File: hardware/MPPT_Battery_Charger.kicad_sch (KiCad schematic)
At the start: 74 parts, among them Q24 SI7414DN-T1-E3, Q25 SI7414DN-T1-E3, Q5 SI7414DN-T1-E3, Q6 SI7414DN-T1-E3, Q8 SI2302DDS-T1-GE3, U22 BQ24650RVAT, U26 LMV321RIYLT, U28 LMV321RIYLT, U4 INA199C1DCKR

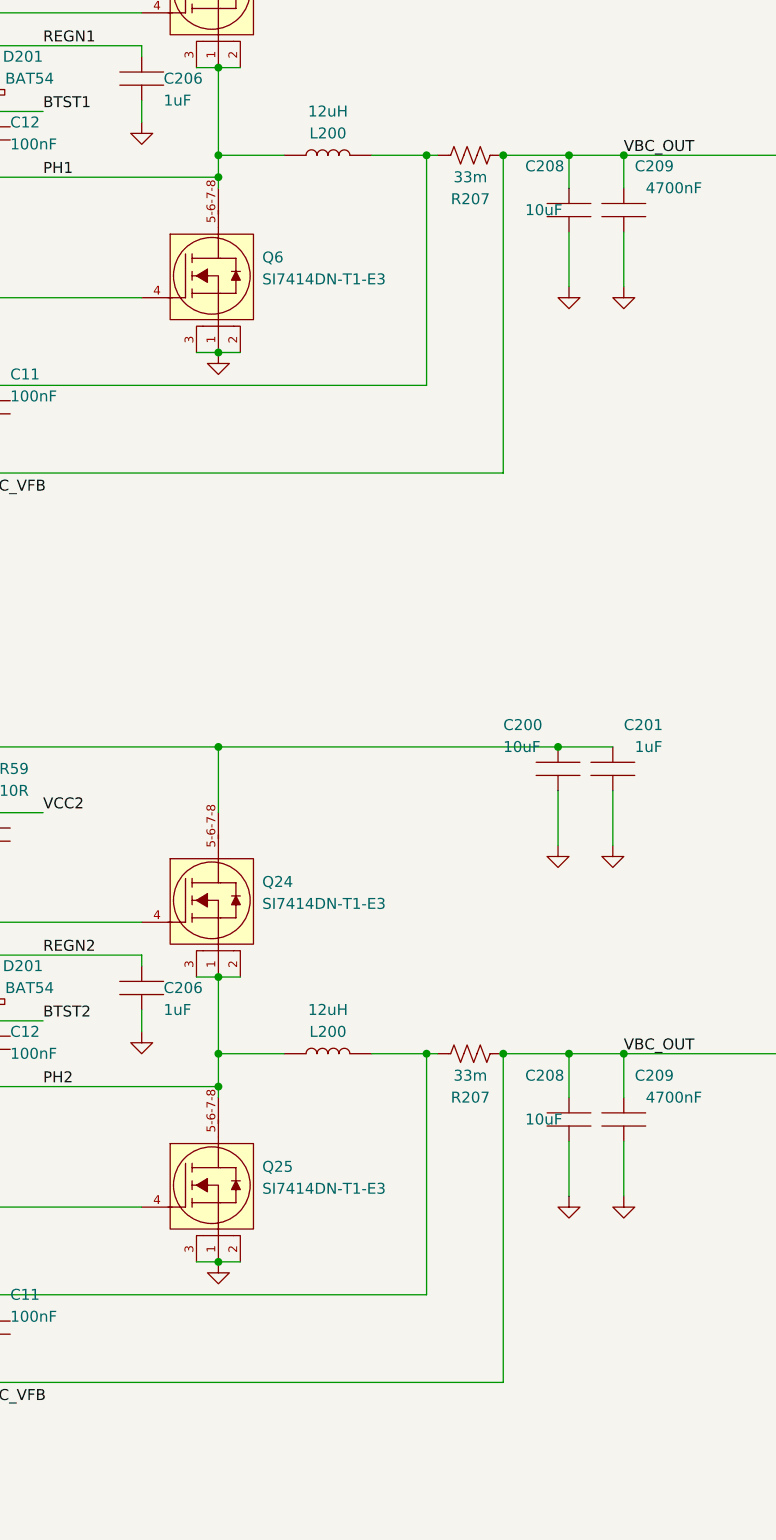
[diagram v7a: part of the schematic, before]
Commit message: hardware: Updating the schematic and layout to solve #8, #9 and #10.
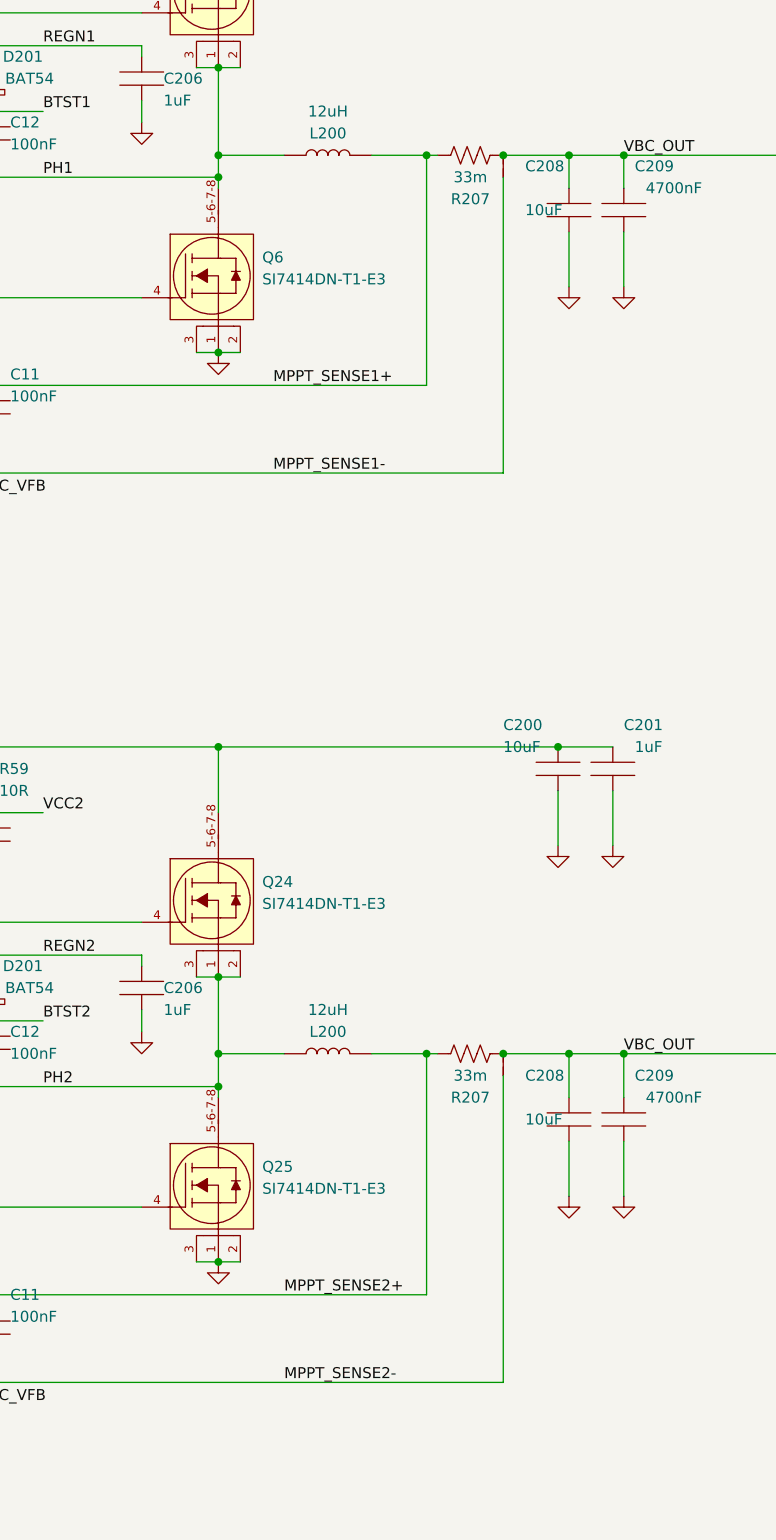
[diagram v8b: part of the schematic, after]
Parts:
- added JP2 (x2): SolderJumper_2_Bridged, footprints:Jumper, symbol Jumper:Jumper
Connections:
- net VBC_OUT: now also JP2.2 (B), JP2.2 (B); no longer C11.2, C11.2, U22.9 (SRN), U22.9 (SRN)
- net MPPT_SENSE1+: now reaches C11.1, L200.2, R207.2, U22.10 (SRP)
- net MPPT_SENSE2+: now reaches C11.1, L200.2, R207.2, U22.10 (SRP)
- new net MPPT_SENSE1-: C11.2, JP2.1 (A), U22.9 (SRN)
- new net MPPT_SENSE2-: C11.2, JP2.1 (A), U22.9 (SRN)
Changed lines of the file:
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@@
     (stroke (width 0) (type default))
   )
-  (wire (pts (xy 256.54 203.2) (xy 256.54 165.1))
+  (wire (pts (xy 256.54 203.2) (xy 256.54 167.64))
     (stroke (width 0) (type default))
   )
@@
     (stroke (width 0) (type default))
   )
-  (wire (pts (xy 256.54 97.79) (xy 256.54 60.96))
+  (wire (pts (xy 256.54 97.79) (xy 256.54 63.5))
     (stroke (width 0) (type default))
   )
@@
     (effects (font (size 1.27 1.27)) (justify left bottom))
   )
+  (label "MPPT_SENSE1-" (at 229.87 97.79 0) (fields_autoplaced)
+    (effects (font (size 1.27 1.27)) (justify left bottom))
+  )
   (label "AMUX3" (at 250.19 264.16 0) (fields_autoplaced)
     (effects (font (size 1.27 1.27)) (justify left bottom))
@@
     (effects (font (size 1.27 1.27)) (justify left bottom))
   )
+  (label "MPPT_SENSE1+" (at 229.87 87.63 0) (fields_autoplaced)
+    (effects (font (size 1.27 1.27)) (justify left bottom))
+  )
   (label "VBC_IN" (at 120.65 85.09 180) (fields_autoplaced)
     (effects (font (size 1.27 1.27)) (justify right bottom))
   )
+  (label "MPPT_SENSE2+" (at 231.14 193.04 0) (fields_autoplaced)
+    (effects (font (size 1.27 1.27)) (justify left bottom))
+  )
   (label "BC_VFB" (at 196.85 205.74 0) (fields_autoplaced)
     (effects (font (size 1.27 1.27)) (justify left bottom))
@@
     (effects (font (size 1.27 1.27)) (justify left bottom))
   )
+  (label "MPPT_SENSE2-" (at 231.14 203.2 0) (fields_autoplaced)
+    (effects (font (size 1.27 1.27)) (justify left bottom))
+  )
   (label "REGN1" (at 203.2 48.26 0) (fields_autoplaced)
     (effects (font (size 1.27 1.27)) (justify left bottom))
@@
     )
   )
+  (symbol (lib_id "Jumper:Jumper") (at 256.54 62.23 90) (unit 1)
+    (in_bom yes) (on_board yes) (dnp no) (fields_autoplaced)
+    (property "Reference" "JP2" (at 254.508 62.23 0)
+      (effects (font (size 1.27 1.27)) hide)
+    )
+    (property "Value" "SolderJumper_2_Bridged" (at 259.08 62.23 0)
+      (effects (font (size 1.27 1.27)) hide)
+    )
+    (property "Footprint" "footprints:Jumper" (at 256.54 62.23 0)
+      (effects (font (size 1.27 1.27)) hide)
+    )
+    (property "Datasheet" "~" (at 256.54 62.23 0)
+      (effects (font (size 1.27 1.27)) hide)
+    )
+    (pin "1")
+    (pin "2")
+    (instances
+      (project "eps-re_project"
+        (path "/2eebaa11-d7ed-4bfd-bc8e-988f68654d29/6cd5fe02-9b19-49bf-9109-b0a2c2f10c14"
+          (reference "JP2") (unit 1)
+        )
+        (path "/2eebaa11-d7ed-4bfd-bc8e-988f68654d29/6f34948c-43a8-4614-b8ed-90c5b6b9b243"
+          (reference "JP4") (unit 1)
+        )
+        (path "/2eebaa11-d7ed-4bfd-bc8e-988f68654d29/0b69622c-4960-45c0-904b-657ff8db02ea"
+          (reference "JP5") (unit 1)
+        )
+      )
+    )
+  )
   (symbol (lib_id "CRCW060330K0FKEAHP:RES") (at 52.07 243.84 90) (unit 1)
     (in_bom yes) (on_board yes) (dnp no)
@@
         )
       )
+    )
+  )
+  (symbol (lib_id "Jumper:Jumper") (at 256.54 166.37 90) (unit 1)
+    (in_bom yes) (on_board yes) (dnp no) (fields_autoplaced)
+    (property "Reference" "JP2" (at 254.508 166.37 0)
+      (effects (font (size 1.27 1.27)) hide)
+    )
+    (property "Value" "SolderJumper_2_Bridged" (at 259.08 166.37 0)
+      (effects (font (size 1.27 1.27)) hide)
+    )
+    (property "Footprint" "footprints:Jumper" (at 256.54 166.37 0)
+      (effects (font (size 1.27 1.27)) hide)
+    )
+    (property "Datasheet" "~" (at 256.54 166.37 0)
+      (effects (font (size 1.27 1.27)) hide)
+    )
+    (pin "1")
+    (pin "2")
+    (instances
+      (project "eps-re_project"
+        (path "/2eebaa11-d7ed-4bfd-bc8e-988f68654d29/6cd5fe02-9b19-49bf-9109-b0a2c2f10c14"
+          (reference "JP2") (unit 1)
+        )
+        (path "/2eebaa11-d7ed-4bfd-bc8e-988f68654d29/6f34948c-43a8-4614-b8ed-90c5b6b9b243"
+          (reference "JP4") (unit 1)
+        )
+        (path "/2eebaa11-d7ed-4bfd-bc8e-988f68654d29/0b69622c-4960-45c0-904b-657ff8db02ea"
+          (reference "JP6") (unit 1)
+        )
+      )
